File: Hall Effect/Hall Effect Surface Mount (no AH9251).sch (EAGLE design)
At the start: 6 parts

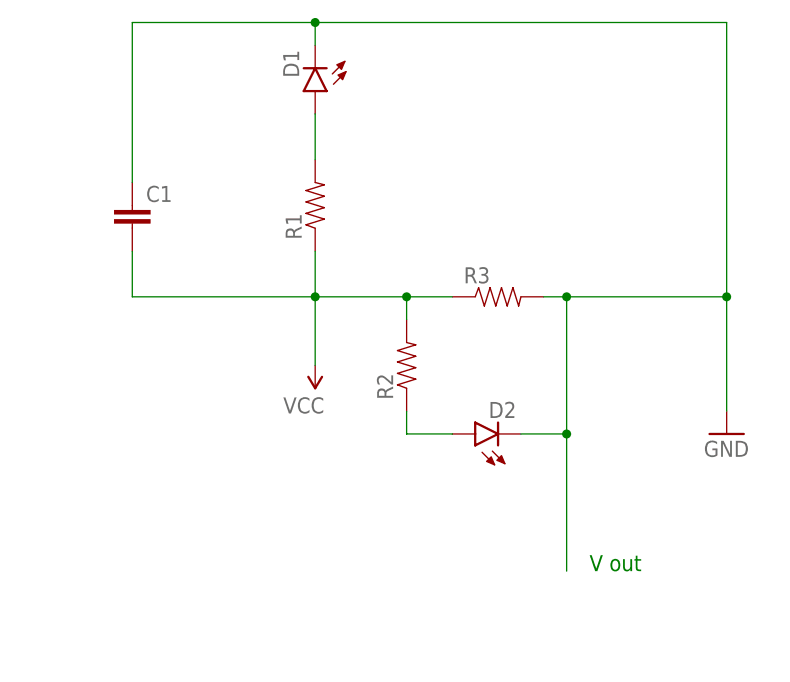
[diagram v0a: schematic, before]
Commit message: Completed schematic with correct part for sensor. Added component values
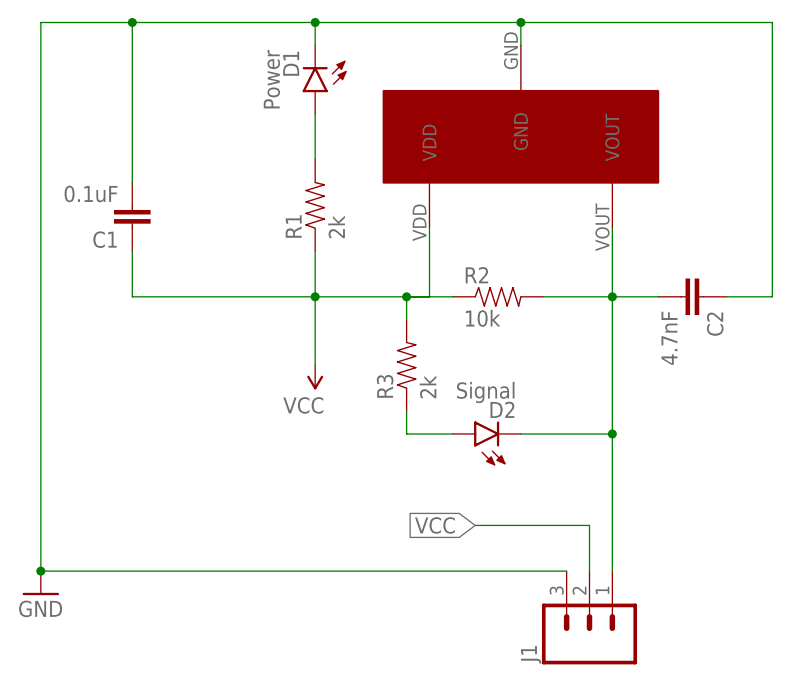
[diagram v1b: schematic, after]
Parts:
- added C2: 4.7nF, SparkFun-Passives:CAP0603-CAP
- added J1: (no value), SparkFun-Connectors:M03PTH
- added U$1: US5881-HALL-EFFECT, TPS5430:US5881-HALL-EFFECT
- C1: value (none) -> 0.1uF; device SparkFun-Capacitors:CAP0402-CAP -> SparkFun-Passives:CAP0603-CAP
- D1: value (none) -> Power; device SparkFun-LED:LED-3MM-NO_SILK -> SparkFun-LED:LED0603
- D2: value (none) -> Signal; device SparkFun-LED:LED-3MM-NO_SILK -> SparkFun-LED:LED0603
- R1, R3: value (none) -> 2k; device SparkFun-Passives:RESISTOR0402-RES -> SparkFun-Passives:RESISTOR0603-RES
- R2: value (none) -> 10k; device SparkFun-Passives:RESISTOR0402-RES -> SparkFun-Passives:RESISTOR0603-RES
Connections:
- new net N$3: C2.2, D2.C, J1.1, R2.2, U$1.VOUT
- net GND: now also C1.2, C2.1, J1.3, U$1.GND; no longer C1.1, D2.C, R3.2
- net N$2: now also R3.1; no longer R2.1
- net VCC: now also C1.1, J1.2, R2.1, R3.2, U$1.VDD; no longer C1.2, R2.2, R3.1
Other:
- note removed: "V out"
- moved on the sheet: C1, R2, R3
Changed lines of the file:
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@@
 <?xml version="1.0" encoding="utf-8"?>
 <!DOCTYPE eagle SYSTEM "eagle.dtd">
-<eagle version="7.6.0">
+<eagle version="7.1.0">
 <drawing>
 <settings>
@@
 <layer number="112" name="tSilk" color="7" fill="1" visible="yes" active="yes"/>
 <layer number="113" name="IDFDebug" color="4" fill="1" visible="yes" active="yes"/>
+<layer number="114" name="Badge_Outline" color="7" fill="1" visible="yes" active="yes"/>
+<layer number="115" name="ReferenceISLANDS" color="7" fill="1" visible="yes" active="yes"/>
 <layer number="116" name="Patch_BOT" color="9" fill="4" visible="yes" active="yes"/>
 <layer number="118" name="Rect_Pads" color="7" fill="1" visible="yes" active="yes"/>
@@
 <parts>
 <part name="SUPPLY1" library="SparkFun-Aesthetics" deviceset="VCC" device=""/>
-<part name="D1" library="SparkFun-LED" deviceset="LED" device="-3MM-NO_SILK"/>
-<part name="C1" library="SparkFun-Capacitors" deviceset="CAP" device="0402-CAP"/>
-<part name="R1" library="SparkFun-Passives" deviceset="RESISTOR" device="0402-RES"/>
-<part name="R2" library="SparkFun-Passives" deviceset="RESISTOR" device="0402-RES"/>
-<part name="R3" library="SparkFun-Passives" deviceset="RESISTOR" device="0402-RES"/>
 <part name="GND1" library="SparkFun-Aesthetics" deviceset="GND" device=""/>
-<part name="D2" library="SparkFun-LED" deviceset="LED" device="-3MM-NO_SILK"/>
+<part name="U$1" library="TPS5430" deviceset="US5881-HALL-EFFECT" device=""/>
+<part name="R1" library="SparkFun-Passives" deviceset="RESISTOR" device="0603-RES" value="2k"/>
+<part name="R2" library="SparkFun-Passives" deviceset="RESISTOR" device="0603-RES" value="10k"/>
+<part name="R3" library="SparkFun-Passives" deviceset="RESISTOR" device="0603-RES" value="2k"/>
+<part name="C1" library="SparkFun-Passives" deviceset="CAP" device="0603-CAP" value="0.1uF"/>
+<part name="C2" library="SparkFun-Passives" deviceset="CAP" device="0603-CAP" value="4.7nF"/>
+<part name="D1" library="SparkFun-LED" deviceset="LED" device="0603" value="Power"/>
+<part name="D2" library="SparkFun-LED" deviceset="LED" device="0603" value="Signal"/>
+<part name="J1" library="SparkFun-Connectors" deviceset="M03" device="PTH"/>
 </parts>
 <sheets>
 <sheet>
 <plain>
-<text x="66.04" y="-2.54" size="1.778" layer="91">V out</text>
 </plain>
 <instances>
 <instance part="SUPPLY1" gate="G$1" x="35.56" y="20.32" rot="R180"/>
+<instance part="GND1" gate="1" x="5.08" y="-5.08"/>
+<instance part="U$1" gate="G$1" x="58.42" y="45.72"/>
+<instance part="R1" gate="G$1" x="35.56" y="38.1" rot="R90"/>
+<instance part="R2" gate="G$1" x="55.88" y="27.94"/>
+<instance part="R3" gate="G$1" x="45.72" y="20.32" rot="R90"/>
+<instance part="C1" gate="G$1" x="15.24" y="38.1" rot="R180"/>
+<instance part="C2" gate="G$1" x="76.2" y="27.94" rot="R270"/>
 <instance part="D1" gate="G$1" x="35.56" y="50.8" rot="R180"/>
-<instance part="C1" gate="G$1" x="15.24" y="35.56"/>
-<instance part="R1" gate="G$1" x="35.56" y="38.1" rot="R90"/>
-<instance part="R2" gate="G$1" x="45.72" y="20.32" rot="R90"/>
-<instance part="R3" gate="G$1" x="55.88" y="27.94"/>
-<instance part="GND1" gate="1" x="81.28" y="12.7"/>
 <instance part="D2" gate="G$1" x="53.34" y="12.7" rot="R90"/>
+<instance part="J1" gate="J$1" x="66.04" y="-10.16" rot="R90"/>
 </instances>
 <busses>
@@
 <segment>
 <pinref part="SUPPLY1" gate="G$1" pin="VCC"/>
-<pinref part="R1" gate="G$1" pin="1"/>
 <wire x1="35.56" y1="20.32" x2="35.56" y2="27.94" width="0.1524" layer="91"/>
-<pinref part="C1" gate="G$1" pin="2"/>
 <wire x1="35.56" y1="27.94" x2="35.56" y2="33.02" width="0.1524" layer="91"/>
 <wire x1="35.56" y1="27.94" x2="15.24" y2="27.94" width="0.1524" layer="91"/>
 <wire x1="15.24" y1="27.94" x2="15.24" y2="33.02" width="0.1524" layer="91"/>
 <junction x="35.56" y="27.94"/>
-<pinref part="R3" gate="G$1" pin="1"/>
 <wire x1="35.56" y1="27.94" x2="45.72" y2="27.94" width="0.1524" layer="91"/>
-<pinref part="R2" gate="G$1" pin="2"/>
 <wire x1="45.72" y1="27.94" x2="50.8" y2="27.94" width="0.1524" layer="91"/>
 <wire x1="45.72" y1="25.4" x2="45.72" y2="27.94" width="0.1524" layer="91"/>
 <junction x="45.72" y="27.94"/>
+<pinref part="R1" gate="G$1" pin="1"/>
+<pinref part="R2" gate="G$1" pin="1"/>
+<pinref part="R3" gate="G$1" pin="2"/>
+<pinref part="C1" gate="G$1" pin="1"/>
+<pinref part="U$1" gate="G$1" pin="VDD"/>
+<wire x1="45.72" y1="27.94" x2="48.26" y2="27.94" width="0.1524" layer="91"/>
+<wire x1="48.26" y1="27.94" x2="48.26" y2="35.56" width="0.1524" layer="91"/>
+</segment>
+<segment>
+<pinref part="J1" gate="J$1" pin="2"/>
+<wire x1="66.04" y1="-2.54" x2="66.04" y2="2.54" width="0.1524" layer="91"/>
+<wire x1="66.04" y1="2.54" x2="53.34" y2="2.54" width="0.1524" layer="91"/>
+<label x="53.34" y="2.54" size="1.778" layer="95" rot="R180" xref="yes"/>
 </segment>
 </net>
 <net name="N$1" class="0">
 <segment>
+<wire x1="35.56" y1="43.18" x2="35.56" y2="48.26" width="0.1524" layer="91"/>
 <pinref part="R1" gate="G$1" pin="2"/>
 <pinref part="D1" gate="G$1" pin="A"/>
-<wire x1="35.56" y1="43.18" x2="35.56" y2="48.26" width="0.1524" layer="91"/>
+</segment>
+</net>
+<net name="N$2" class="0">
+<segment>
+<wire x1="45.72" y1="15.24" x2="45.72" y2="12.7" width="0.1524" layer="91"/>
+<wire x1="45.72" y1="12.7" x2="50.8" y2="12.7" width="0.1524" layer="91"/>
+<pinref part="R3" gate="G$1" pin="1"/>
+<pinref part="D2" gate="G$1" pin="A"/>
+</segment>
+</net>
+<net name="N$3" class="0">
+<segment>
+<pinref part="R2" gate="G$1" pin="2"/>
+<wire x1="60.96" y1="27.94" x2="68.58" y2="27.94" width="0.1524" layer="91"/>
+<wire x1="68.58" y1="27.94" x2="68.58" y2="12.7" width="0.1524" layer="91"/>
+<pinref part="D2" gate="G$1" pin="C"/>
+<wire x1="58.42" y1="12.7" x2="68.58" y2="12.7" width="0.1524" layer="91"/>
+<junction x="68.58" y="12.7"/>
+<wire x1="68.58" y1="12.7" x2="68.58" y2="-2.54" width="0.1524" layer="91"/>
+<pinref part="C2" gate="G$1" pin="2"/>
+<wire x1="68.58" y1="27.94" x2="73.66" y2="27.94" width="0.1524" layer="91"/>
+<junction x="68.58" y="27.94"/>
+<pinref part="U$1" gate="G$1" pin="VOUT"/>
+<wire x1="68.58" y1="35.56" x2="68.58" y2="27.94" width="0.1524" layer="91"/>
+<pinref part="J1" gate="J$1" pin="1"/>
 </segment>
 </net>
 <net name="GND" class="0">
 <segment>
-<pinref part="R3" gate="G$1" pin="2"/>
-<wire x1="60.96" y1="27.94" x2="63.5" y2="27.94" width="0.1524" layer="91"/>
-<wire x1="63.5" y1="27.94" x2="63.5" y2="12.7" width="0.1524" layer="91"/>
-<pinref part="C1" gate="G$1" pin="1"/>
-<wire x1="63.5" y1="12.7" x2="63.5" y2="-2.54" width="0.1524" layer="91"/>
 <wire x1="15.24" y1="40.64" x2="15.24" y2="58.42" width="0.1524" layer="91"/>
 <wire x1="15.24" y1="58.42" x2="35.56" y2="58.42" width="0.1524" layer="91"/>
-<wire x1="35.56" y1="58.42" x2="81.28" y2="58.42" width="0.1524" layer="91"/>
-<wire x1="81.28" y1="58.42" x2="81.28" y2="27.94" width="0.1524" layer="91"/>
-<pinref part="D1" gate="G$1" pin="C"/>
+<wire x1="35.56" y1="58.42" x2="58.42" y2="58.42" width="0.1524" layer="91"/>
+<wire x1="58.42" y1="58.42" x2="86.36" y2="58.42" width="0.1524" layer="91"/>
+<wire x1="86.36" y1="58.42" x2="86.36" y2="27.94" width="0.1524" layer="91"/>
 <wire x1="35.56" y1="55.88" x2="35.56" y2="58.42" width="0.1524" layer="91"/>
 <junction x="35.56" y="58.42"/>
-<wire x1="63.5" y1="27.94" x2="81.28" y2="27.94" width="0.1524" layer="91"/>
-<junction x="63.5" y="27.94"/>
-<wire x1="81.28" y1="27.94" x2="81.28" y2="15.24" width="0.1524" layer="91"/>
-<junction x="81.28" y="27.94"/>
+<pinref part="C1" gate="G$1" pin="2"/>
+<pinref part="D1" gate="G$1" pin="C"/>
+<pinref part="C2" gate="G$1" pin="1"/>
+<wire x1="81.28" y1="27.94" x2="86.36" y2="27.94" width="0.1524" layer="91"/>
+<pinref part="U$1" gate="G$1" pin="GND"/>
+<wire x1="58.42" y1="55.88" x2="58.42" y2="58.42" width="0.1524" layer="91"/>
+<junction x="58.42" y="58.42"/>
+<wire x1="15.24" y1="58.42" x2="5.08" y2="58.42" width="0.1524" layer="91"/>
+<wire x1="5.08" y1="58.42" x2="5.08" y2="-2.54" width="0.1524" layer="91"/>
+<junction x="15.24" y="58.42"/>
 <pinref part="GND1" gate="1" pin="GND"/>
-<pinref part="D2" gate="G$1" pin="C"/>
-<wire x1="58.42" y1="12.7" x2="63.5" y2="12.7" width="0.1524" layer="91"/>
-<junction x="63.5" y="12.7"/>
-</segment>
-</net>
-<net name="N$2" class="0">
-<segment>
-<pinref part="R2" gate="G$1" pin="1"/>
-<wire x1="45.72" y1="15.24" x2="45.72" y2="12.7" width="0.1524" layer="91"/>
-<pinref part="D2" gate="G$1" pin="A"/>
-<wire x1="45.72" y1="12.7" x2="50.8" y2="12.7" width="0.1524" layer="91"/>
-</segment>
-</net>
+<pinref part="J1" gate="J$1" pin="3"/>
+<wire x1="5.08" y1="-2.54" x2="63.5" y2="-2.54" width="0.1524" layer="91"/>
+<junction x="5.08" y="-2.54"/>
+</segment>
+</net>
